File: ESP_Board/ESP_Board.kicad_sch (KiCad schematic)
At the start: 16 parts, among them U1 ESP32-S3, Y1 C1E-40.000-8-1010-R

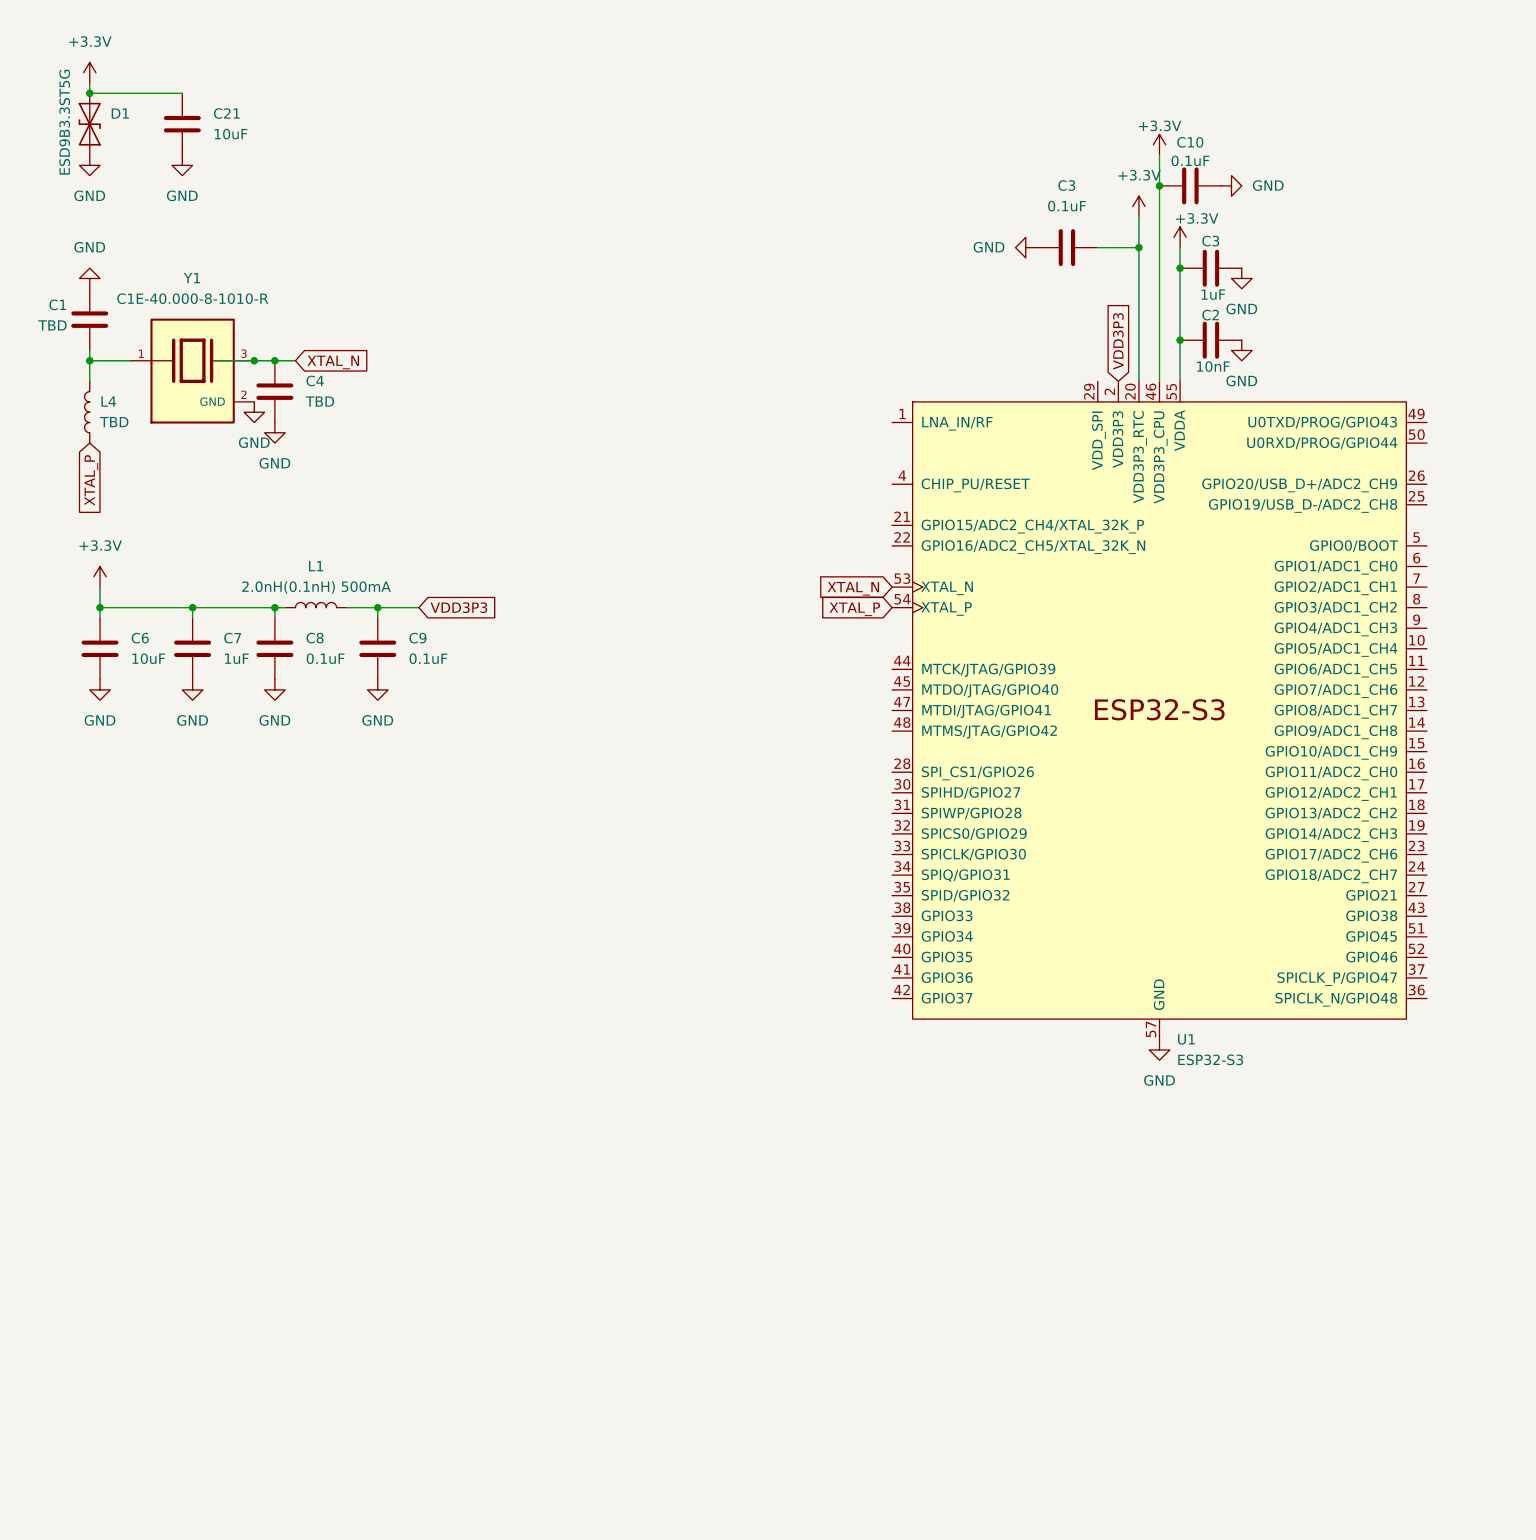
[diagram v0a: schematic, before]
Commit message: Add voltage regulator & USB-C to ESP board
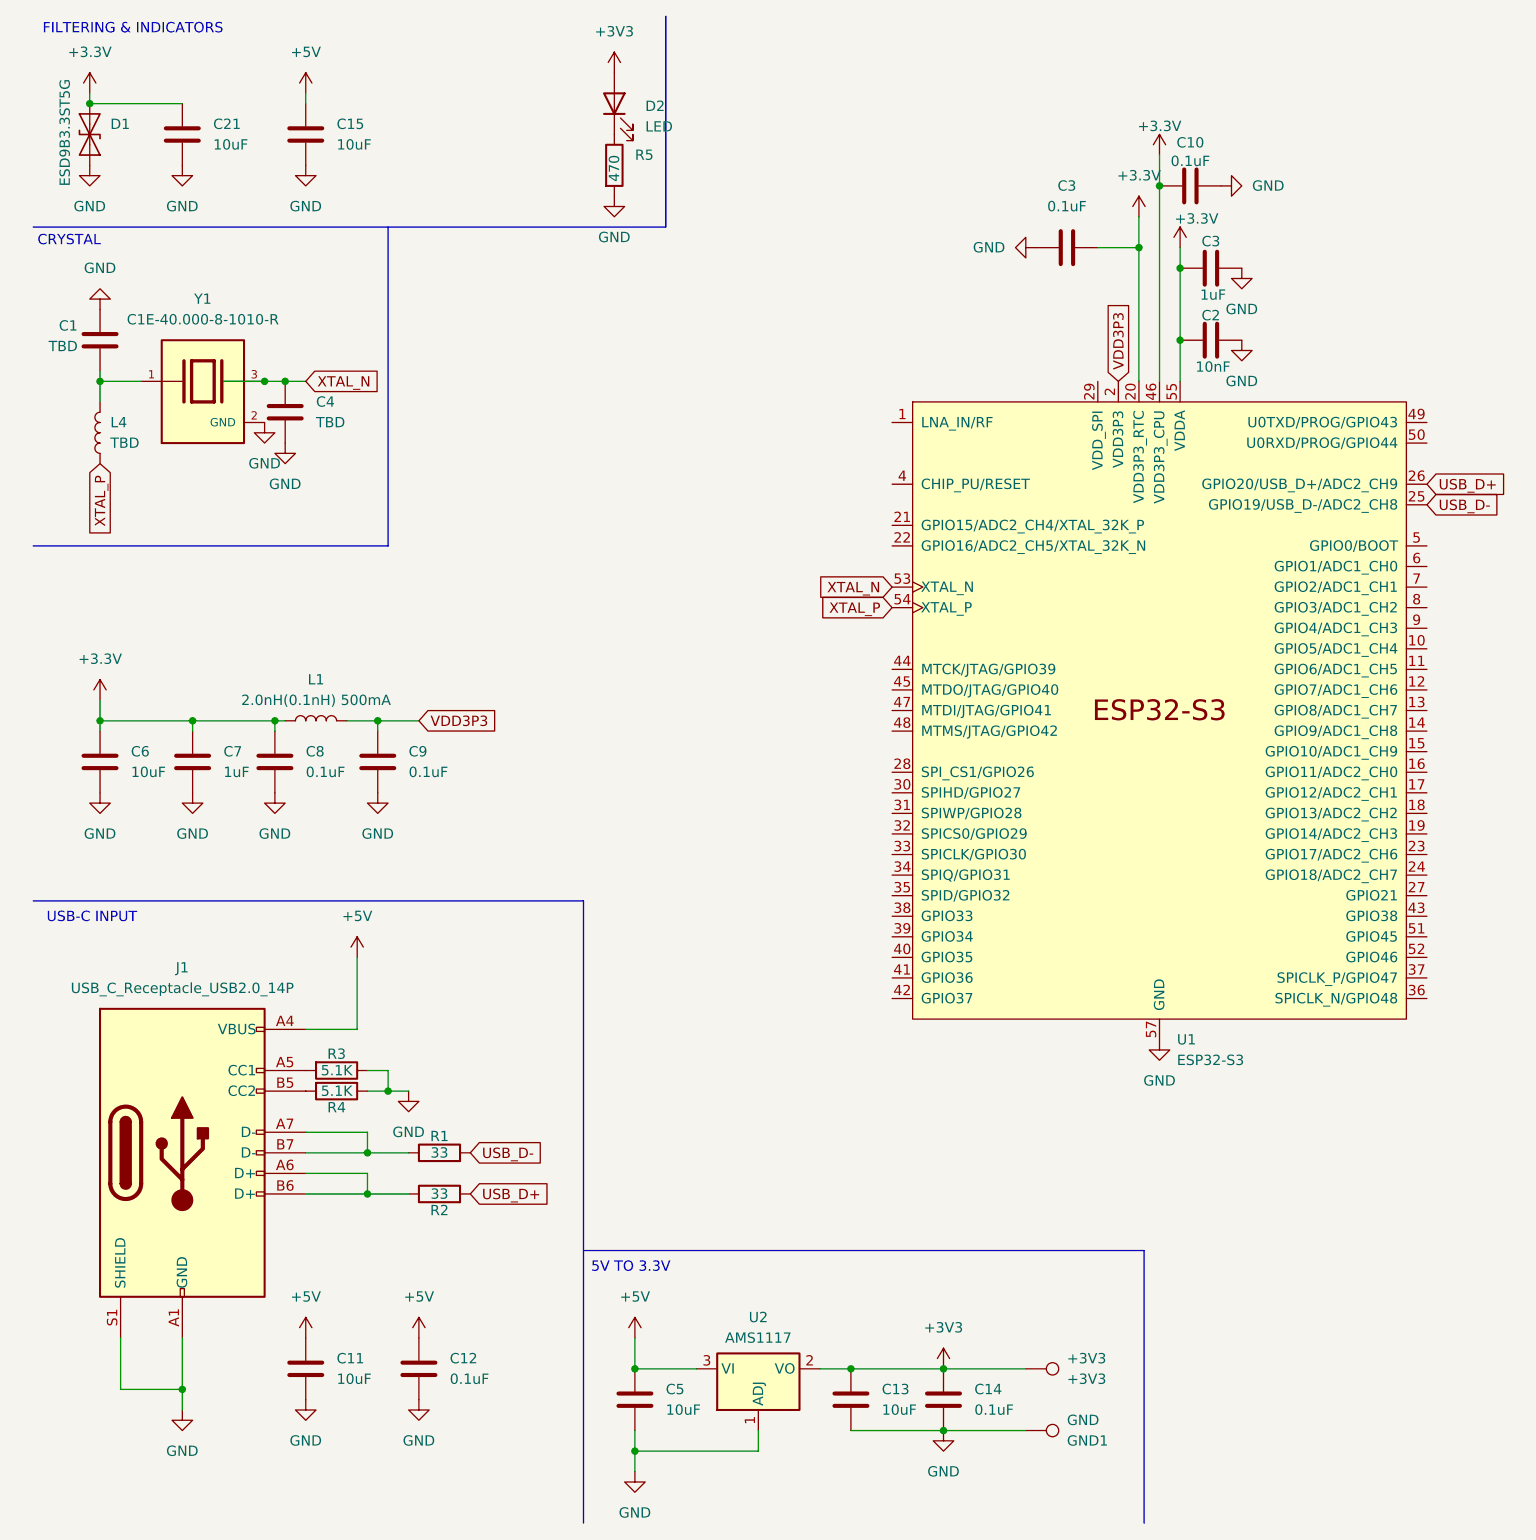
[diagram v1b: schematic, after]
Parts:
- added +3V3: +3V3, symbol Connector:TestPoint
- added C11, C13, C15, C5: 10uF, symbol Device:C
- added C12, C14: 0.1uF, symbol Device:C
- added D2: LED, symbol Device:LED
- added GND: GND1, symbol Connector:TestPoint
- added J1: USB_C_Receptacle_USB2.0_14P, symbol Connector:USB_C_Receptacle_USB2.0_14P
- added R1, R2: 33, symbol Device:R
- added R3, R4: 5.1K, symbol Device:R
- added R5: 470, symbol Device:R
- added U2: AMS1117, Package_TO_SOT_SMD:SOT-223-3_TabPin2, symbol Regulator_Linear:AMS1117
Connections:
- net GND: now also C11.2, C12.2, C13.2, C14.2, C15.2, C5.2, GND.1, J1.A1 (GND), J1.A12 (GND), J1.B1 (GND), J1.B12 (GND), J1.S1 (SHIELD), R3.1, R4.1, R5.2, U2.1 (ADJ)
- net USB_D-: now reaches U1.25 (GPIO19/USB_D-/ADC2_CH8)
- net USB_D-: now also R1.2
- net USB_D+: now reaches U1.26 (GPIO20/USB_D+/ADC2_CH9)
- net USB_D+: now also R2.2
- new net: D2.1 (K), R5.1
- new net: J1.A5 (CC1), R3.2
- new net: J1.A6 (D+), J1.B6 (D+), R2.1
- new net: J1.A7 (D-), J1.B7 (D-), R1.1
- new net: J1.B5 (CC2), R4.2
- new net +3V3: +3V3.1, C13.1, C14.1, D2.2 (A), U2.2 (VO)
- new net +5V: C11.1, C12.1, C15.1, C5.1, J1.A4 (VBUS), J1.A9 (VBUS), J1.B4 (VBUS), J1.B9 (VBUS), U2.3 (VI)
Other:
- note added: "5V TO 3.3V"
- note added: "CRYSTAL"
- note added: "FILTERING & INDICATORS"
- note added: "USB-C INPUT"
- moved on the sheet: C1, C21, C4, C6, C7, C8, C9, D1, L1, L4, Y1

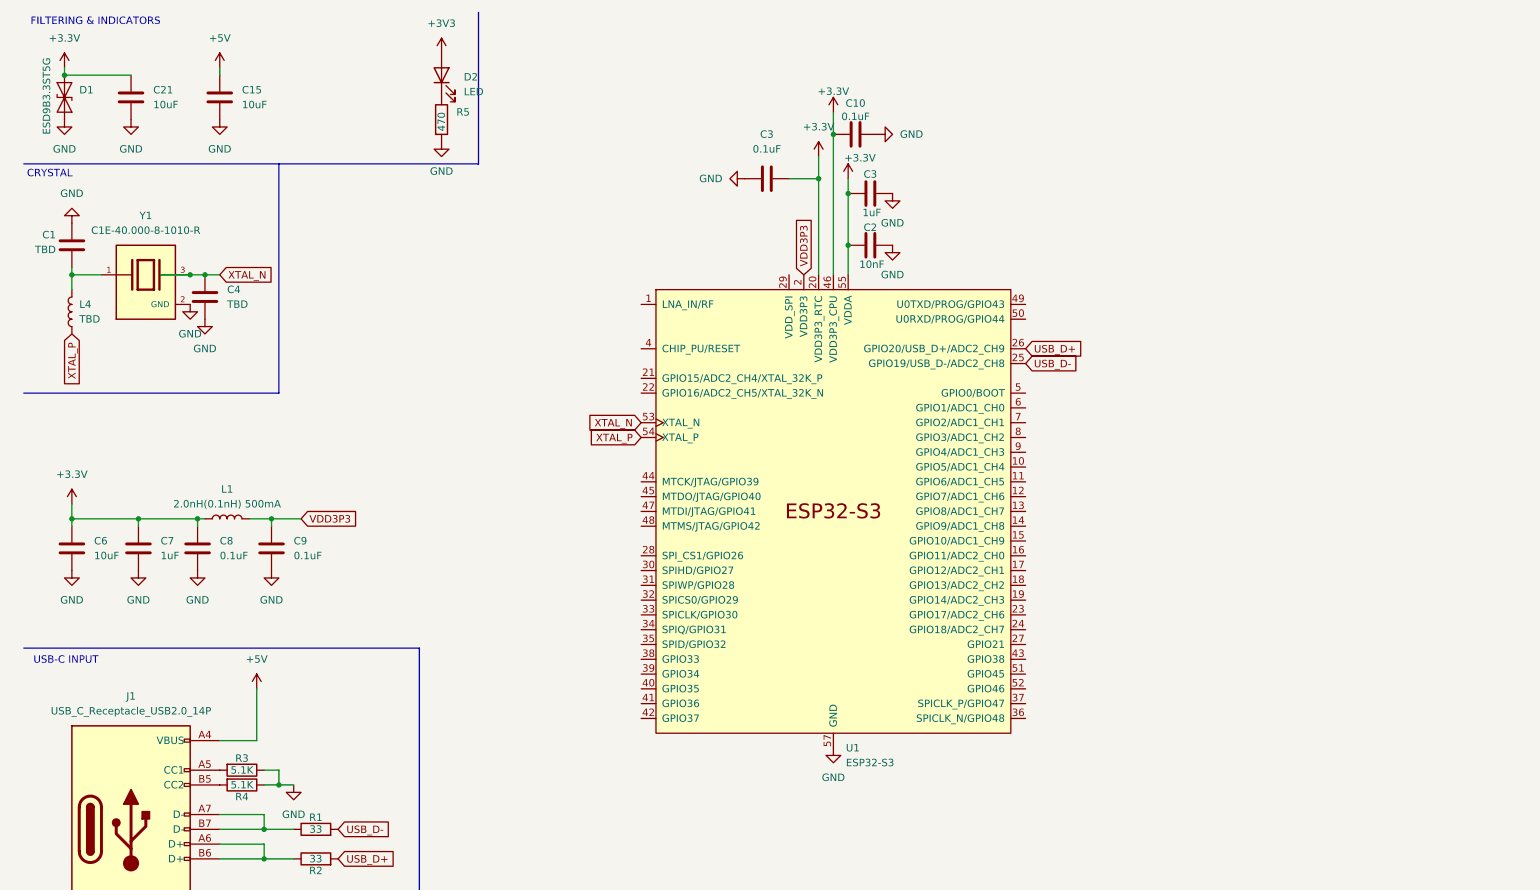
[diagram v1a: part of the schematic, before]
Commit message: Add more smoothing capacitors, reset button
Still need to add antenna, outputs, 32k crystal, & memory
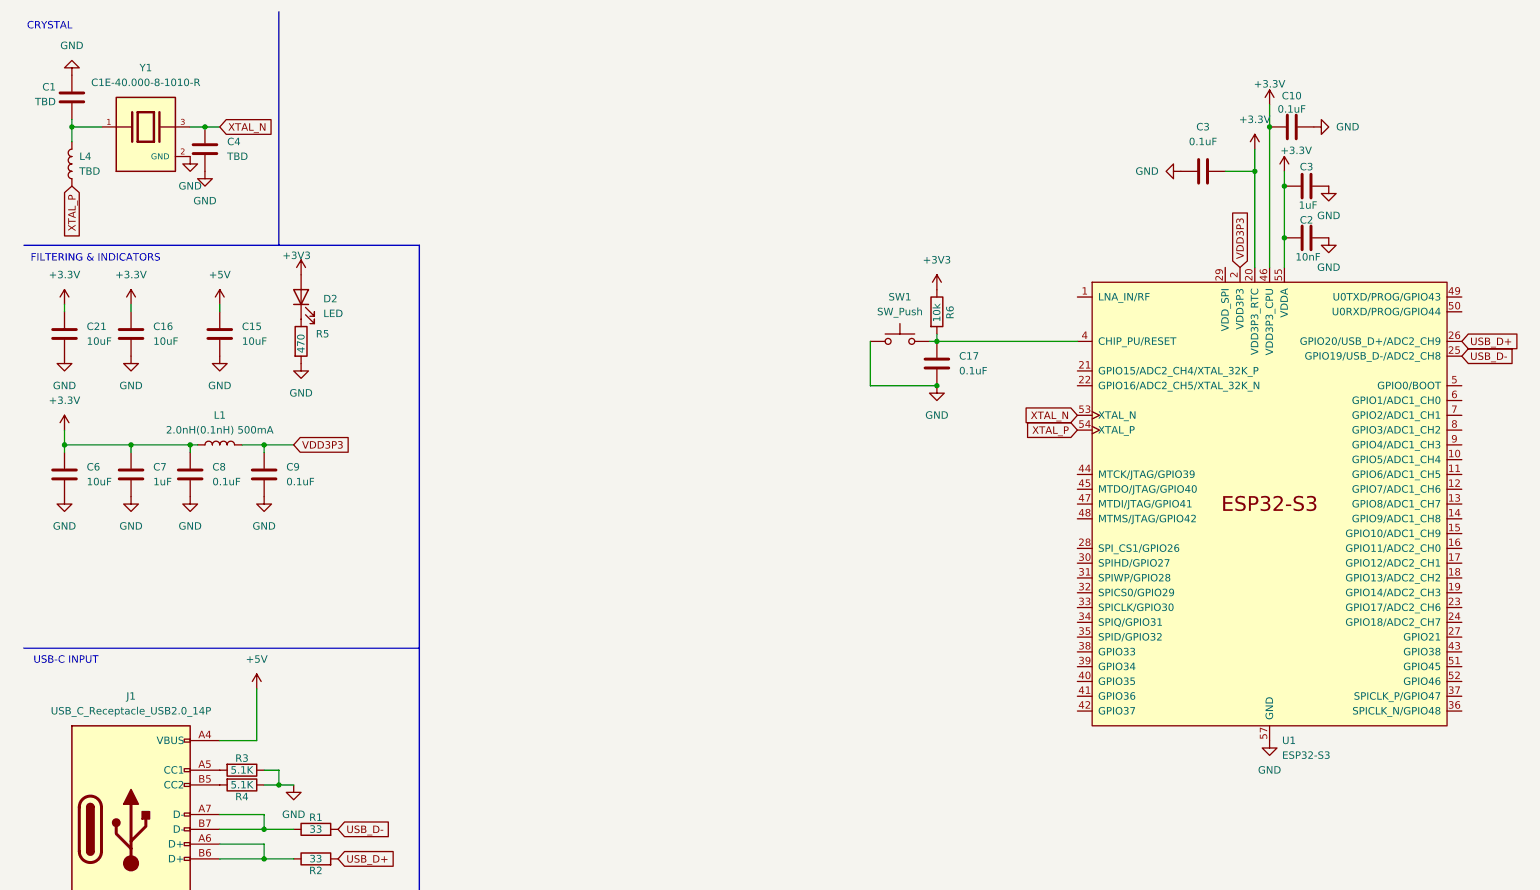
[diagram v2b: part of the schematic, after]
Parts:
- removed D1: ESD9B3.3ST5G, Diode_SMD:D_SOD-923, symbol Diode:ESD9B3.3ST5G
- added C16: 10uF, symbol Device:C
- added C17: 0.1uF, symbol Device:C
- added R6: 10k, symbol Device:R
- added SW1: SW_Push, symbol Switch:SW_Push
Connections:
- net +3.3V: now also C16.1
- net +3V3: now also R6.1
- net GND: now also C16.2, C17.2, SW1.1
- net at U1.4 (CHIP_PU/RESET): now also C17.1, R6.2, SW1.2
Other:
- moved on the sheet: 1uF, C1, C10, C15, C2, C21, C3, C4, C6, C7, C8, C9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

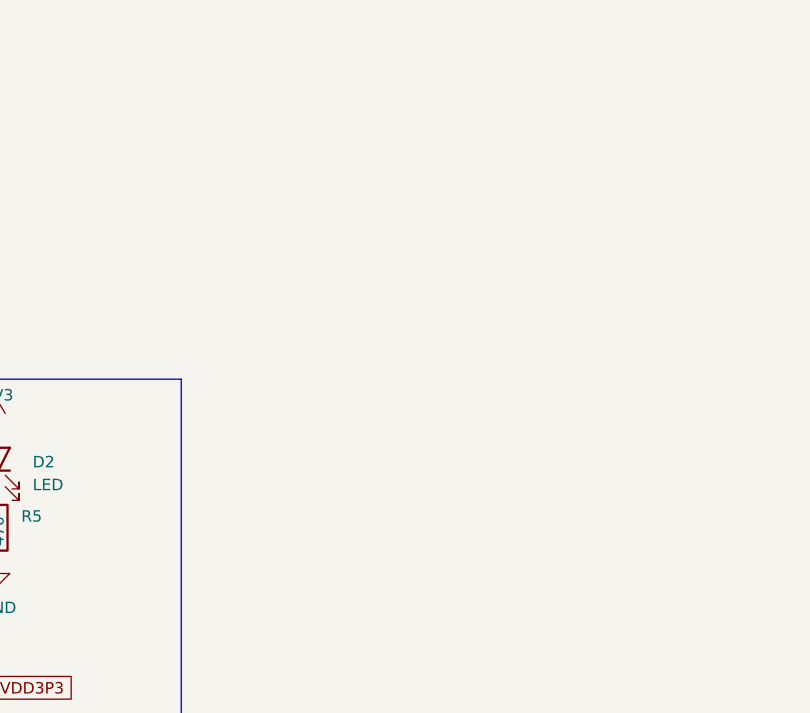
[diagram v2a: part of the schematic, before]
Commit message: Add a ton of IO outputs
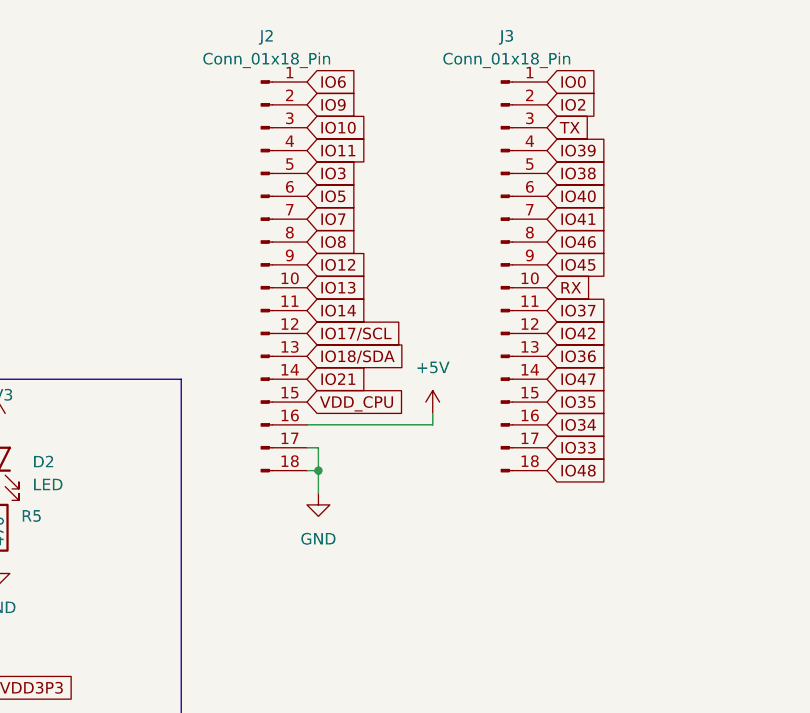
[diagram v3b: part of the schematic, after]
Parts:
- added J2, J3: Conn_01x18_Pin, symbol Connector:Conn_01x18_Pin
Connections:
- net +5V: now also J2.16 (Pin_16)
- net GND: now also J2.17 (Pin_17), J2.18 (Pin_18)
- new net IO0: J3.1 (Pin_1)
- new net IO10: J2.3 (Pin_3)
- new net IO11: J2.4 (Pin_4)
- new net IO12: J2.9 (Pin_9)
- new net IO13: J2.10 (Pin_10)
- new net IO14: J2.11 (Pin_11)
- new net IO17/SCL: J2.12 (Pin_12)
- new net IO18/SDA: J2.13 (Pin_13)
- new net IO2: J3.2 (Pin_2)
- new net IO21: J2.14 (Pin_14)
- new net IO3: J2.5 (Pin_5)
- new net IO33: J3.17 (Pin_17)
- new net IO34: J3.16 (Pin_16)
- new net IO35: J3.15 (Pin_15)
- new net IO36: J3.13 (Pin_13)
- new net IO37: J3.11 (Pin_11)
- new net IO38: J3.5 (Pin_5)
- new net IO39: J3.4 (Pin_4)
- new net IO40: J3.6 (Pin_6)
- new net IO41: J3.7 (Pin_7)
- new net IO42: J3.12 (Pin_12)
- new net IO45: J3.9 (Pin_9)
- new net IO46: J3.8 (Pin_8)
- new net IO47: J3.14 (Pin_14)
- new net IO48: J3.18 (Pin_18)
- new net IO5: J2.6 (Pin_6)
- new net IO6: J2.1 (Pin_1)
- new net IO7: J2.7 (Pin_7)
- new net IO8: J2.8 (Pin_8)
- new net IO9: J2.2 (Pin_2)
- new net RX: J3.10 (Pin_10)
- new net TX: J3.3 (Pin_3)
- new net VDD_CPU: J2.15 (Pin_15)
